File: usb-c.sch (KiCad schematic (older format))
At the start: 55 parts, among them J201 USB_C, U201 PTN5110HQZ, U202 PTN36043BXY, U203 TLV3201AIDBVR, U204 PCMF3HDMI2SZ, U205 PCMF2HDMI2SZ

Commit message: Re-labelled signals around USB-C with naming scheme for differential routing (_P/_N names). Routed some data lines behind USB connector.
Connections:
- net labels added: RX_CON_1_N, RX_CON_1_P, RX_CON_2_N, RX_CON_2_P, TX_CON_1C_N, TX_CON_1C_P, TX_CON_1_N, TX_CON_1_P, TX_CON_2C_N, TX_CON_2C_P, TX_CON_2_N, TX_CON_2_P, USB1_RXC_N, USB1_RXC_P
- wire segments 252 -> 263
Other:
- moved on the sheet: C201, C202, C207, C208, C209, C210, C211, C212, D201, D202, R201, R202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

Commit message: Make some minor aesthetic adjustments to the USB-C schematic sheet, the USB-C receptacle symbol should come from the dvk-mx8m-bsb library
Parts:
- J201: symbol USB_C_Receptacle-RESCUE-dvk-mx8m-bsb -> USB-C_Receptacle
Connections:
- wire segments 263 -> 249
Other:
- moved on the sheet: C201, C202, C207, C208, C211, C212, D201, R201, R202, R203, R204, R205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

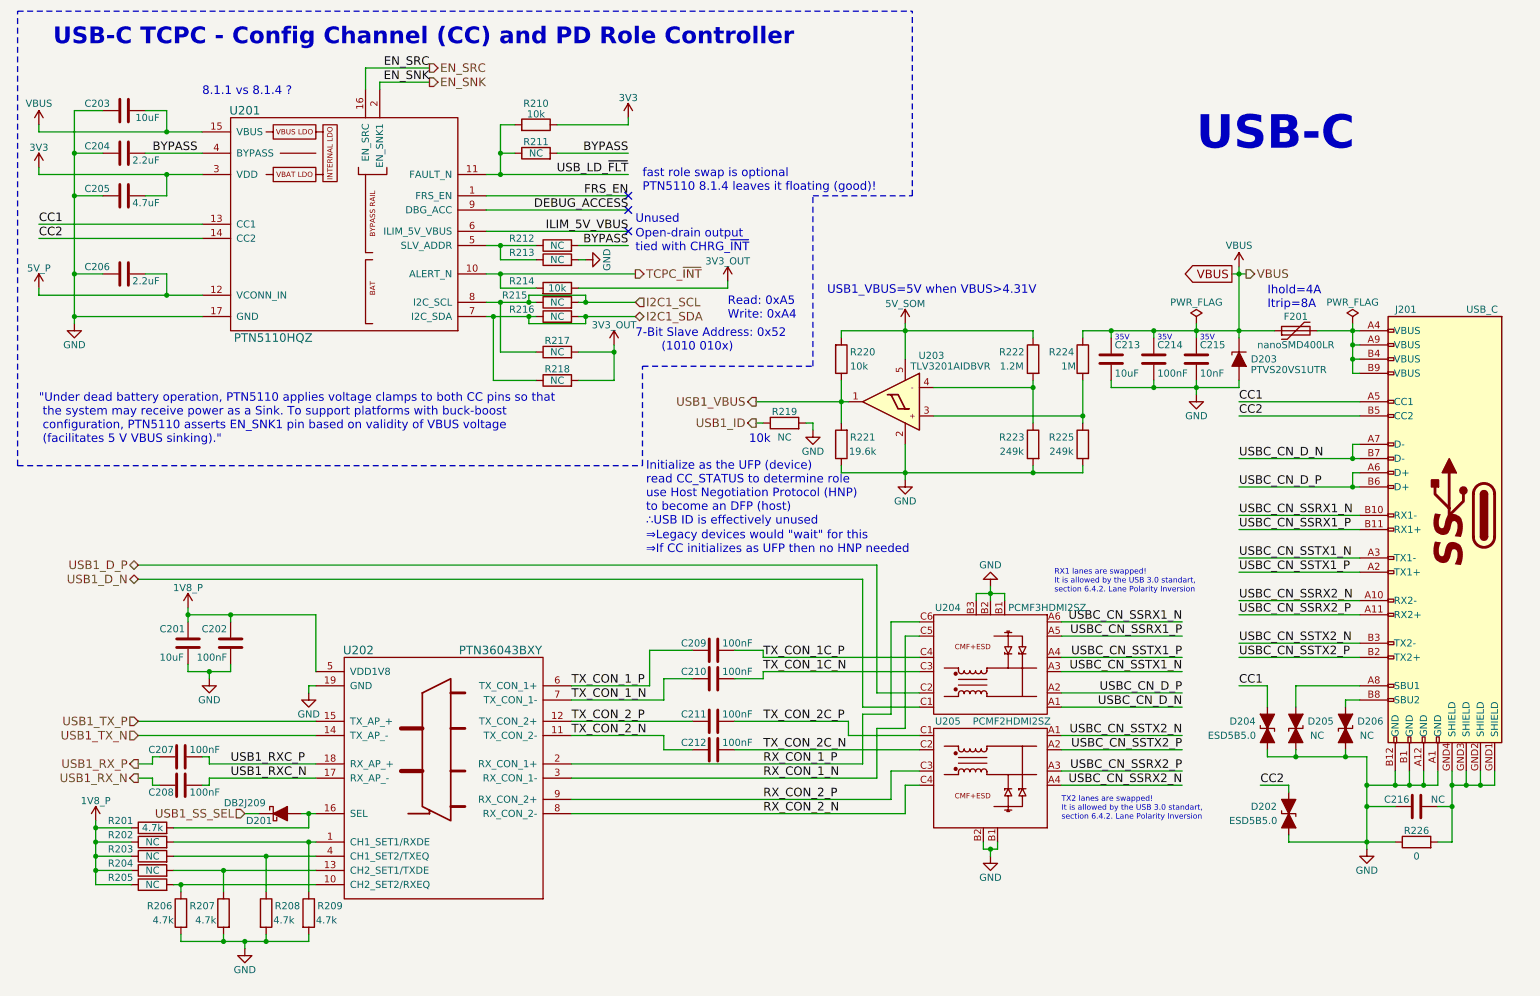
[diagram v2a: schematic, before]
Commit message: Route the PTC polyfuse that's on the VBUS rail using a copper pour on the In4.Cu layer, route the USB-C's shielding to parallel 0Ohm and NC cap to GND, add a power net class, add a 0.508mm annular ring 0.254mm drill via for power nets
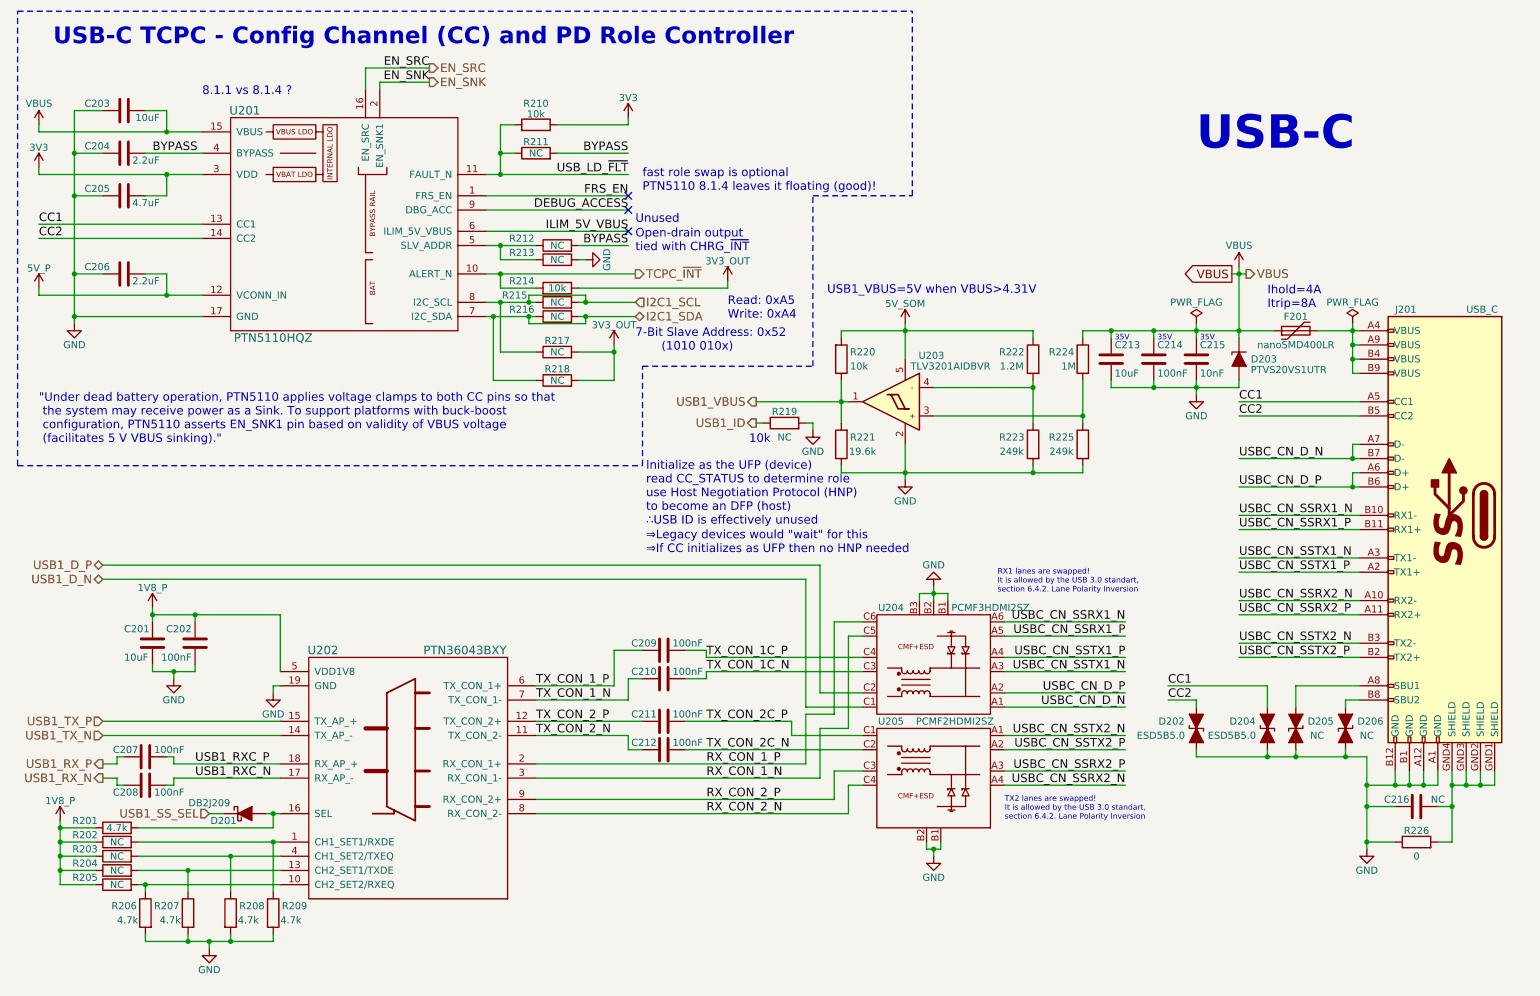
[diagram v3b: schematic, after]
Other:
- moved on the sheet: C201, C202, C207, C208, C209, C210, C211, C212, D201, D202, R201, R202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

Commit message: Move the VBUS TVS diode and bypass caps and place copper pour on the respective pad areas, the VBUS rail has a 6mm wide fill zone in order to properly handle ~4.3A with a <10degreeC temperature rise (should also do this when bring VBUS to the charge controller), make the In4.Cu layer a solid ground layer
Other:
- note added: "RX1 lanes are swapped!\nIt is allowed by the USB 3.0 standard,\nsection 6.4.2. Lane Polarity Inversion"
- note added: "TX2 lanes are swapped!\nIt is allowed by the USB 3.0 standard,\nsection 6.4.2. Lane Polarity Inversion"
- note removed: "RX1 lanes are swapped!\nIt is allowed by the USB 3.0 standart,\nsection 6.4.2. Lane Polarity Inversion"
- note removed: "TX2 lanes are swapped!\nIt is allowed by the USB 3.0 standart,\nsection 6.4.2. Lane Polarity Inversion"
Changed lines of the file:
@@
 USB-C
 Text Notes 7400 4600 0    39   ~ 0
-RX1 lanes are swapped!\nIt is allowed by the USB 3.0 standart,\nsection 6.4.2. Lane Polarity Inversion
+RX1 lanes are swapped!\nIt is allowed by the USB 3.0 standard,\nsection 6.4.2. Lane Polarity Inversion
 Text Notes 7450 6200 0    39   ~ 0
-TX2 lanes are swapped!\nIt is allowed by the USB 3.0 standart,\nsection 6.4.2. Lane Polarity Inversion
+TX2 lanes are swapped!\nIt is allowed by the USB 3.0 standard,\nsection 6.4.2. Lane Polarity Inversion
 $Comp
 L USB-C_Receptacle J201

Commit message: Use I2C3 bus instead of I2C1 bus based on EmCraft's feedback
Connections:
- net I2C1_SCL renamed I2C3_SCL
- net I2C1_SDA renamed I2C3_SDA
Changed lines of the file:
@@
 EN_SRC
 Text HLabel 4850 2550 2    60   Input ~ 0
-I2C1_SCL
+I2C3_SCL
 Text HLabel 4850 2650 2    60   BiDi ~ 0
-I2C1_SDA
+I2C3_SDA
 Text HLabel 4850 2350 2    60   Output ~ 0
 TCPC_~INT

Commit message: Move the charge controller, USB-C TCPC, and RTC to I2C1
Since each of these ICs will be powered at the same time as the SoM regardless of the PWR_EN state, they should share the same I2C bus as the PMIC.
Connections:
- net I2C3_SCL renamed I2C1_SCL
- net I2C3_SDA renamed I2C1_SDA
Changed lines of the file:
@@
 $EndComp
 $Comp
-L GND #PWR027
+L GND #PWR028
 U 1 1 5ADED127
 P 4500 2250
-F 0 "#PWR027" H 4500 2000 50  0001 C CNN
+F 0 "#PWR028" H 4500 2000 50  0001 C CNN
 F 1 "GND" H 4500 2100 50  0000 C CNN
 F 2 "" H 4500 2250 50  0001 C CNN
@@
 $EndComp
 $Comp
-L 3V3_OUT #PWR028
+L 3V3_OUT #PWR029
 U 1 1 5ADED151
 P 4700 2850
-F 0 "#PWR028" H 4700 2700 50  0001 C CNN
+F 0 "#PWR029" H 4700 2700 50  0001 C CNN
 F 1 "3V3_OUT" H 4700 2990 50  0000 C CNN
 F 2 "" H 4700 2850 50  0001 C CNN
@@
 $EndComp
 $Comp
-L 3V3_OUT #PWR029
+L 3V3_OUT #PWR030
 U 1 1 5ADED157
 P 5500 2400
-F 0 "#PWR029" H 5500 2250 50  0001 C CNN
+F 0 "#PWR030" H 5500 2250 50  0001 C CNN
 F 1 "3V3_OUT" H 5500 2540 50  0000 C CNN
 F 2 "" H 5500 2400 50  0001 C CNN
@@
 $EndComp
 $Comp
-L GND #PWR030
+L GND #PWR031
 U 1 1 5ADED15E
 P 900 2700
-F 0 "#PWR030" H 900 2450 50  0001 C CNN
+F 0 "#PWR031" H 900 2450 50  0001 C CNN
 F 1 "GND" H 900 2550 50  0000 C CNN
 F 2 "" H 900 2700 50  0001 C CNN
@@
 EN_SRC
 Text HLabel 4850 2550 2    60   Input ~ 0
-I2C3_SCL
+I2C1_SCL
 Text HLabel 4850 2650 2    60   BiDi ~ 0
-I2C3_SDA
+I2C1_SDA
 Text HLabel 4850 2350 2    60   Output ~ 0
 TCPC_~INT
@@
 USB-C TCPC - Config Channel (CC) and PD Role Controller
 $Comp
-L GND #PWR031
+L GND #PWR032
 U 1 1 5AECC278
 P 2300 5300
-F 0 "#PWR031" H 2300 5050 50  0001 C CNN
+F 0 "#PWR032" H 2300 5050 50  0001 C CNN
 F 1 "GND" H 2300 5150 50  0000 C CNN
 F 2 "" H 2300 5300 50  0001 C CNN
@@
 $EndComp
 $Comp
-L GND #PWR032
+L GND #PWR033
 U 1 1 5AED260D
 P 1600 5200
-F 0 "#PWR032" H 1600 4950 50  0001 C CNN
+F 0 "#PWR033" H 1600 4950 50  0001 C CNN
 F 1 "GND" H 1600 5050 50  0000 C CNN
 F 2 "" H 1600 5200 50  0001 C CNN
@@
 $EndComp
 $Comp
-L GND #PWR033
+L GND #PWR034
 U 1 1 5AED9A25
 P 1850 7100
-F 0 "#PWR033" H 1850 6850 50  0001 C CNN
+F 0 "#PWR034" H 1850 6850 50  0001 C CNN
 F 1 "GND" H 1850 6950 50  0000 C CNN
 F 2 "" H 1850 7100 50  0001 C CNN
@@
 $EndComp
 $Comp
-L 1V8_P #PWR034
+L 1V8_P #PWR035
 U 1 1 5AEE2251
 P 800 6200
-F 0 "#PWR034" H 800 6050 50  0001 C CNN
+F 0 "#PWR035" H 800 6050 50  0001 C CNN
 F 1 "1V8_P" H 800 6340 50  0000 C CNN
 F 2 "" H 800 6200 50  0001 C CNN
@@
 $EndComp
 $Comp
-L GND #PWR035
+L GND #PWR036
 U 1 1 5AF3BA54
 P 8800 3200
-F 0 "#PWR035" H 8800 2950 50  0001 C CNN
+F 0 "#PWR036" H 8800 2950 50  0001 C CNN
 F 1 "GND" H 8800 3050 50  0000 C CNN
 F 2 "" H 8800 3200 50  0001 C CNN
@@
 $EndComp
 $Comp
-L GND #PWR036
+L GND #PWR037
 U 1 1 5AF4F7E8
 P 6750 3800
-F 0 "#PWR036" H 6750 3550 50  0001 C CNN
+F 0 "#PWR037" H 6750 3550 50  0001 C CNN
 F 1 "GND" H 6750 3650 50  0000 C CNN
 F 2 "" H 6750 3800 50  0001 C CNN
@@
 $EndComp
 $Comp
-L GND #PWR037
+L GND #PWR038
 U 1 1 5AF595A0
 P 6100 3450
-F 0 "#PWR037" H 6100 3200 50  0001 C CNN
+F 0 "#PWR038" H 6100 3200 50  0001 C CNN
 F 1 "GND" H 6100 3300 50  0000 C CNN
 F 2 "" H 6100 3450 50  0001 C CNN
@@
 $EndComp
 $Comp
-L GND #PWR038
+L GND #PWR039
 U 1 1 5AF8A55A
 P 6950 6450
-F 0 "#PWR038" H 6950 6200 50  0001 C CNN
+F 0 "#PWR039" H 6950 6200 50  0001 C CNN
 F 1 "GND" H 6950 6300 50  0000 C CNN
 F 2 "" H 6950 6450 50  0001 C CNN
@@
 $EndComp
 $Comp
-L GND #PWR039
+L GND #PWR040
 U 1 1 5AF8A8ED
 P 6950 4550
-F 0 "#PWR039" H 6950 4300 50  0001 C CNN
+F 0 "#PWR040" H 6950 4300 50  0001 C CNN
 F 1 "GND" H 6950 4400 50  0000 C CNN
 F 2 "" H 6950 4550 50  0001 C CNN
@@
 $EndComp
 $Comp
-L GND #PWR040
+L GND #PWR041
 U 1 1 5AFA9EDB
 P 10000 6400
-F 0 "#PWR040" H 10000 6150 50  0001 C CNN
+F 0 "#PWR041" H 10000 6150 50  0001 C CNN
 F 1 "GND" H 10000 6250 50  0000 C CNN
 F 2 "" H 10000 6400 50  0001 C CNN
@@
 NoConn ~ 4800 1900
 $Comp
-L 1V8_P #PWR041
+L 1V8_P #PWR042
 U 1 1 5B02622C
 P 1450 4700
-F 0 "#PWR041" H 1450 4550 50  0001 C CNN
+F 0 "#PWR042" H 1450 4550 50  0001 C CNN
 F 1 "1V8_P" H 1450 4840 50  0000 C CNN
 F 2 "" H 1450 4700 50  0001 C CNN
@@
 USB1_VBUS=5V when VBUS>4.31V
 $Comp
-L VBUS #PWR042
+L VBUS #PWR043
 U 1 1 5AF2D1E1
 P 9100 2300
-F 0 "#PWR042" H 9100 2150 50  0001 C CNN
+F 0 "#PWR043" H 9100 2150 50  0001 C CNN
 F 1 "VBUS" H 9100 2450 50  0000 C CNN
 F 2 "" H 9100 2300 50  0001 C CNN
@@
 $EndComp
 $Comp
-L PWR_FLAG #FLG043
+L PWR_FLAG #FLG044
 U 1 1 5AF2D52F
 P 8800 2700
-F 0 "#FLG043" H 8800 2775 50  0001 C CNN
+F 0 "#FLG044" H 8800 2775 50  0001 C CNN
 F 1 "PWR_FLAG" H 8800 2850 50  0000 C CNN
 F 2 "" H 8800 2700 50  0001 C CNN
@@
 NoConn ~ 4800 2050
 $Comp
-L VBUS #PWR044
+L VBUS #PWR045
 U 1 1 5AF6C71F
 P 650 1300
-F 0 "#PWR044" H 650 1150 50  0001 C CNN
+F 0 "#PWR045" H 650 1150 50  0001 C CNN
 F 1 "VBUS" H 650 1450 50  0000 C CNN
 F 2 "" H 650 1300 50  0001 C CNN
@@
 NoConn ~ 4800 1800
 $Comp
-L PWR_FLAG #FLG045
+L PWR_FLAG #FLG046
 U 1 1 5AF77F57
 P 9900 2700
-F 0 "#FLG045" H 9900 2775 50  0001 C CNN
+F 0 "#FLG046" H 9900 2775 50  0001 C CNN
 F 1 "PWR_FLAG" H 9900 2850 50  0000 C CNN
 F 2 "" H 9900 2700 50  0001 C CNN
@@
 VBUS
 $Comp
-L 3V3 #PWR046
+L 3V3 #PWR047
 U 1 1 5B39F466
 P 4800 1250
-F 0 "#PWR046" H 4800 1100 50  0001 C CNN
+F 0 "#PWR047" H 4800 1100 50  0001 C CNN
 F 1 "3V3" H 4800 1390 50  0000 C CNN
 F 2 "" H 4800 1250 50  0001 C CNN
@@
 $EndComp
 $Comp
-L 3V3 #PWR047
+L 3V3 #PWR048
 U 1 1 5B39F890
 P 650 1600
-F 0 "#PWR047" H 650 1450 50  0001 C CNN
+F 0 "#PWR048" H 650 1450 50  0001 C CNN
 F 1 "3V3" H 650 1740 50  0000 C CNN
 F 2 "" H 650 1600 50  0001 C CNN
@@
 $EndComp
 $Comp
-L 5V_P #PWR048
+L 5V_P #PWR049
 U 1 1 5B3E3D9A
 P 650 2450
-F 0 "#PWR048" H 650 2300 50  0001 C CNN
+F 0 "#PWR049" H 650 2300 50  0001 C CNN
 F 1 "5V_P" H 650 2590 50  0000 C CNN
 F 2 "" H 650 2450 50  0001 C CNN
@@
 $EndComp
 $Comp
-L 5V_SOM #PWR049
+L 5V_SOM #PWR050
 U 1 1 5B1A8979
 P 6750 2700
-F 0 "#PWR049" H 6750 2550 50  0001 C CNN
+F 0 "#PWR050" H 6750 2550 50  0001 C CNN
 F 1 "5V_SOM" H 6750 2840 50  0000 C CNN
 F 2 "" H 6750 2700 50  0001 C CNN

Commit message: Update project files to KiCad 5.0.0
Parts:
- C201, C202, C203, C204, C205, C206, C207, C208, C209, C210, C211, C212, C213, C214, C215, C216: symbol C -> dvk-mx8m-bsb-rescue:C
- D201: symbol D_Schottky_ALT -> dvk-mx8m-bsb-rescue:D_Schottky_ALT
- D202, D204, D205, D206: symbol D_TVS_ALT -> dvk-mx8m-bsb-rescue:D_TVS_ALT
- D203: symbol D_Zener_ALT -> dvk-mx8m-bsb-rescue:D_Zener_ALT
- F201: symbol Polyfuse -> dvk-mx8m-bsb-rescue:Polyfuse
- J201: symbol USB-C_Receptacle -> dvk-mx8m-bsb:USB-C_Receptacle
- R201, R202, R203, R204, R205, R206, R207, R208, R209, R210, R211, R212, R213, R214, R215, R216, R217, R218, R219, R220, R221, R222, R223, R224, R225, R226: symbol R -> dvk-mx8m-bsb-rescue:R
- U201: symbol PTN5110HQZ -> dvk-mx8m-bsb:PTN5110HQZ
- U202: symbol PTN36043BXY -> dvk-mx8m-bsb:PTN36043BXY
- U203: symbol TLV3201AIDBVR -> dvk-mx8m-bsb:TLV3201AIDBVR
- U204: symbol PCMF3HDMI2SZ -> dvk-mx8m-bsb:PCMF3HDMI2SZ
- U205: symbol PCMF2HDMI2SZ -> dvk-mx8m-bsb:PCMF2HDMI2SZ
